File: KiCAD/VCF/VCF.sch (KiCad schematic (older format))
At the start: 58 parts, among them J1 Power, J2 MJ-3502, J3 MJ-3502, J4 MJ-3502, Q1 2N3906, Q10 2N3392, Q11 2N3392, Q12 2N3392, Q2 2N3392, Q3 2N3392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

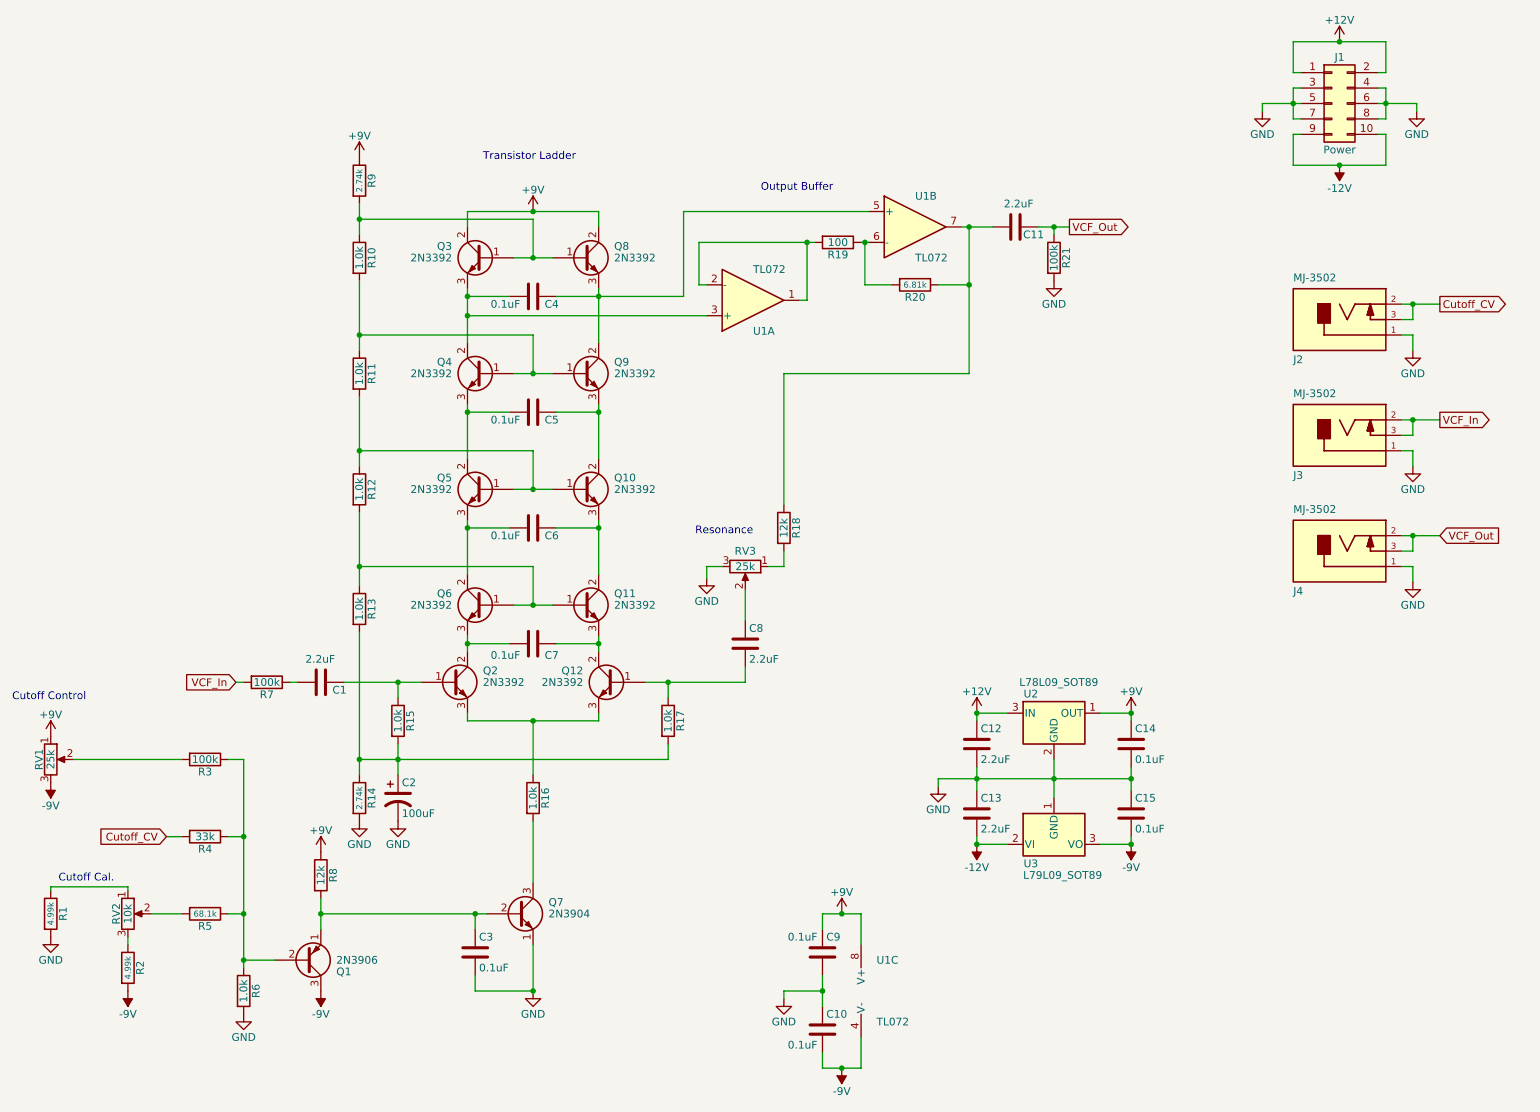
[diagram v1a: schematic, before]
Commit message: Added RevB and VCA
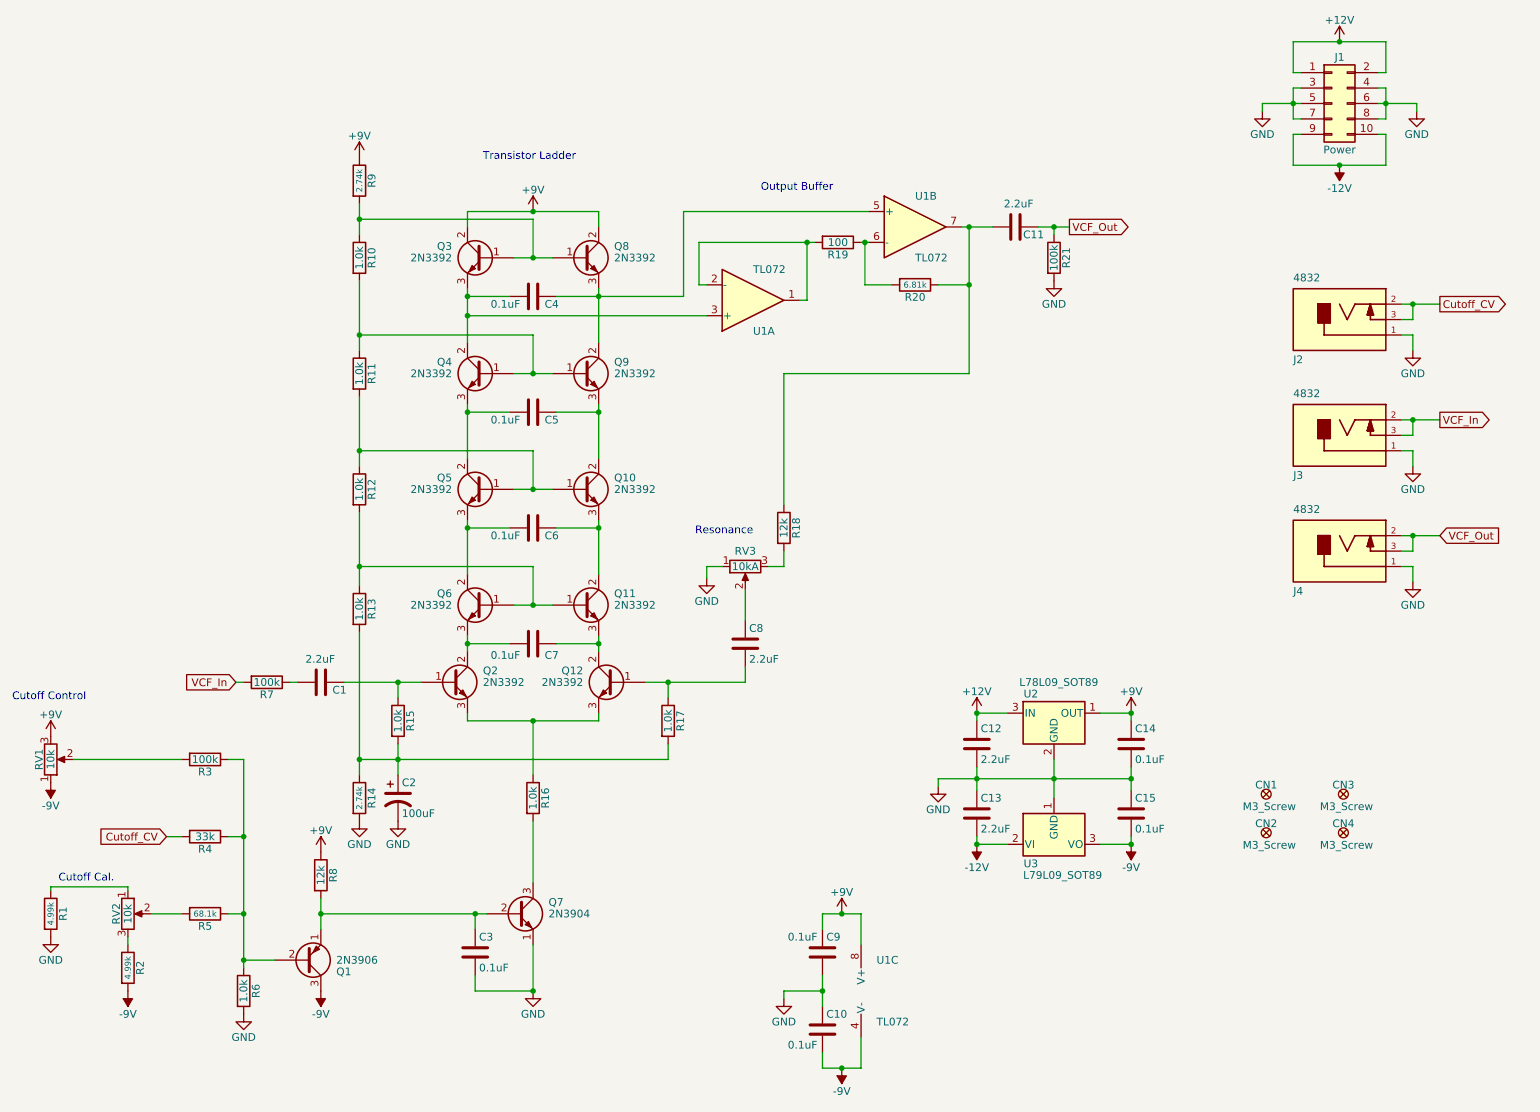
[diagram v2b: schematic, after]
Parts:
- added CN1, CN2, CN3, CN4: M3_Screw, Synth:M3_Screw_Hole, symbol Synth:M3_Screw
- C1, C11, C12, C13, C8: Digikey Link (none) -> https://www.digikey.com/short/p4nfth; Digikey PN (none) -> 1276-1072-1-ND; Unit Price (none) -> 0.22
- C10, C14, C15, C3, C4, C5, C6, C7, C9: Digikey Link (none) -> https://www.digikey.com/short/p4nr3m; Digikey PN (none) -> 720-1540-1-ND; Unit Price (none) -> 0.237
- C2: Digikey Link (none) -> https://www.digikey.com/short/p4nfcn; Digikey PN (none) -> 399-9749-1-ND; Unit Price (none) -> 2.71
- J1: Digikey Link (none) -> https://www.digikey.com/short/p4nr5h; Digikey PN (none) -> 609-3243-ND; Unit Price (none) -> 0.27
- J2, J3, J4: value MJ-3502 -> 4832; footprint Connector_PinHeader_2.54mm:PinHeader_1x02_P2.54mm_Vertical -> Synth:Schurter_4832_Jack; Digikey Link (none) -> https://www.digikey.com/short/p4nr1r; Digikey PN (none) -> 486-3418-ND; Field4 CP-3502MJ-ND -> (none); Field5 None -> (none); Field6 MJ-3502 -> (none); Field7 https://www.cui.com/product/interconnect/connectors/audio-c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 -> (none); Field8 3.5 mm, Mono, Right Angle, Through Hole, Threaded Bushing, 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 -> (none); Field9 CUI Inc. -> (none); Unit Price (none) -> 1.50
- Q1: Digikey Link (none) -> https://www.digikey.com/short/p4nf3t; Digikey PN (none) -> 2N3906TARFSCT-ND; Unit Price (none) -> 0.24
- Q10, Q11, Q12, Q2, Q3, Q4, Q5, Q6, Q8, Q9: Digikey Link (none) -> https://www.digikey.com/short/p4nfcv; Digikey PN (none) -> 2N3392CS-ND; Unit Price (none) -> 0.647
- Q7: Digikey Link (none) -> https://www.digikey.com/short/p4nft0; Digikey PN (none) -> 2N3904FS-ND; Unit Price (none) -> 0.21
- R1, R2: Digikey Link (none) -> https://www.digikey.com/short/p4nf79; Digikey PN (none) -> RNCP1206FTD4K99CT-ND; Unit Price (none) -> 0.10
- R10, R11, R12, R13, R15, R16, R17, R6: Digikey Link (none) -> https://www.digikey.com/short/p4nrdz; Digikey PN (none) -> 311-1.0KERCT-ND; Unit Price (none) -> 0.10
- R14, R9: Digikey Link (none) -> https://www.digikey.com/short/p4nftt; Digikey PN (none) -> 311-2.74KFRCT-ND; Unit Price (none) -> 0.10
- R18, R8: Digikey Link (none) -> https://www.digikey.com/short/p4nf70; Digikey PN (none) -> A129823CT-ND; Unit Price (none) -> 0.10
- R19: Digikey Link (none) -> https://www.digikey.com/short/p4nftq; Digikey PN (none) -> RNCP1206FTD100RCT-ND; Unit Price (none) -> 0.10
- R20: Digikey Link (none) -> https://www.digikey.com/short/p4nft8; Digikey PN (none) -> RNCP1206FTD6K81CT-ND; Unit Price (none) -> 0.10
- R21, R3, R7: Digikey Link (none) -> https://www.digikey.com/short/p4nr28; Digikey PN (none) -> A129834CT-ND; Unit Price (none) -> 0.07
- R4: Digikey Link (none) -> https://www.digikey.com/short/p4nrww; Digikey PN (none) -> RMCF1206JT33K0CT-ND; Unit Price (none) -> 0.10
- R5: Digikey Link (none) -> https://www.digikey.com/short/p4nf72; Digikey PN (none) -> RNCP1206FTD68K1CT-ND; Unit Price (none) -> 0.10
- RV1: value 25k -> 10k; footprint Connector_PinHeader_2.54mm:PinHeader_1x03_P2.54mm_Vertical -> Synth:Potentiometer_Bourns_PTV09A-1_Single_Vertical; Digikey Link (none) -> https://www.digikey.com/short/p4nf35; Digikey PN (none) -> PTV09A-4020F-B103-ND; Unit Price (none) -> 0.83
- RV2: Digikey Link (none) -> https://www.digikey.com/short/p4nrbh; Digikey PN (none) -> 1993-1104-ND; Unit Price (none) -> 0.46
- RV3: value 25k -> 10kA; footprint Connector_PinHeader_2.54mm:PinHeader_1x03_P2.54mm_Vertical -> Synth:Potentiometer_Bourns_PTV09A-1_Single_Vertical; Digikey Link (none) -> https://www.digikey.com/short/p4nf3v; Digikey PN (none) -> PTV09A-4020F-A103-ND; Unit Price (none) -> 0.83
- U1: Digikey Link (none) -> https://www.digikey.com/short/p4nf7q; Digikey PN (none) -> 296-1282-1-ND; Unit Price (none) -> 0.62
- U2: Digikey Link (none) -> https://www.digikey.com/short/p4nftn; Digikey PN (none) -> 497-1192-1-ND; Unit Price (none) -> 0.42
- U3: Digikey Link (none) -> https://www.digikey.com/short/p4nftb; Digikey PN (none) -> NJM79L09UA-TE1CT-ND; Unit Price (none) -> 0.80
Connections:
- net +9V: now also RV1.3; no longer RV1.1
- net -9V: now also RV1.1; no longer RV1.3
- net GND: now also RV3.1; no longer RV3.3
- net at R18.2: now also RV3.3; no longer RV3.1
